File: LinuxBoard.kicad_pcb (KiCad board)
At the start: 2 copper layers, 182 parts, among them J1 Wuerth_7499010121A, J2 Conn_02x10_Counter_Clockwise, J3 Micro_SD_Card, J4 USB_A, J5 Conn_ARM_JTAG_SWD_20, J6 USB_B_Micro, SW1 SW_DIP_x03, SW2 SW_Push, SW3 SW_Push, SW4 SW_Push, SW5 SW_Push, U1 STM32MP151AAB3, U2 MT41K64M16TW-107_AAT_J_TR, U3 DP83848C, U4 STPMIC1APQR, Y1 24MHz, Y2 32.768KHz, Y2 Crystal_GND24, Y3 25MHz

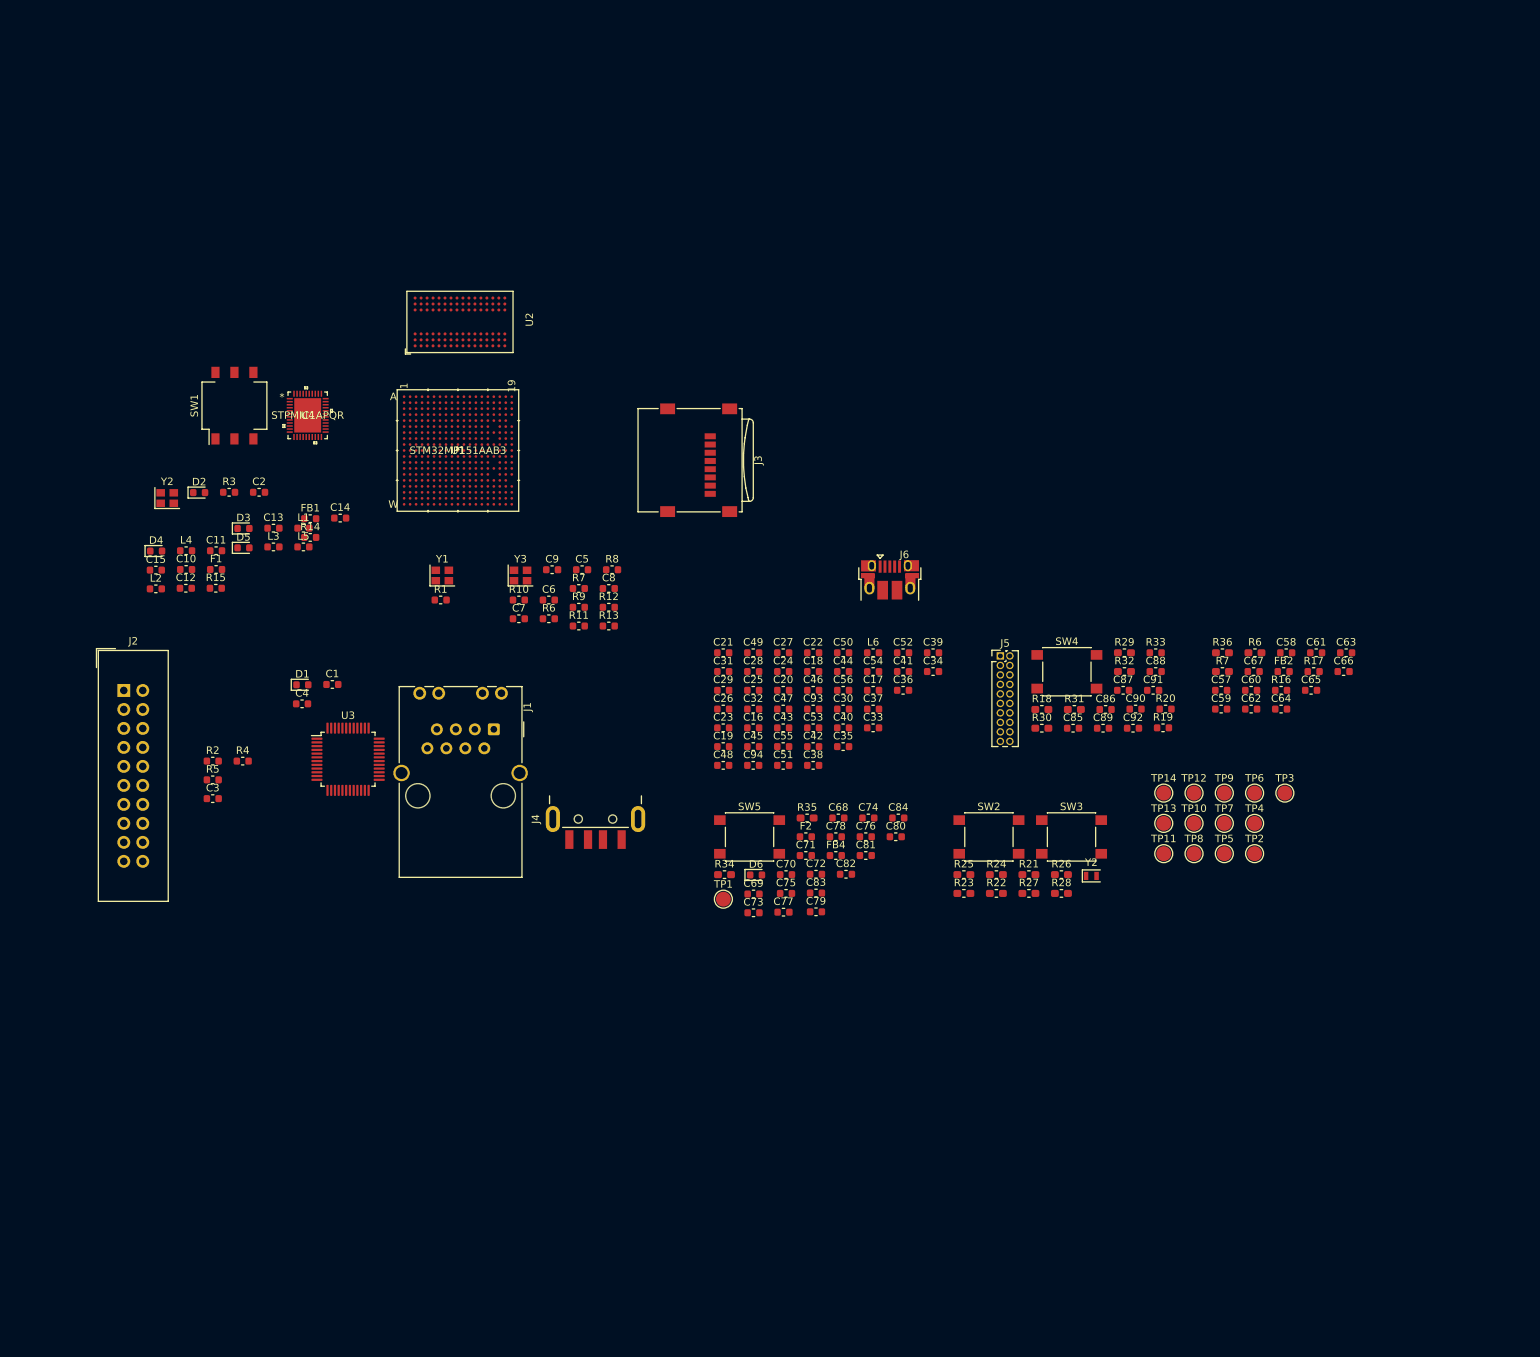
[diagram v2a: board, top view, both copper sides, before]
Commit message: Update jtag connector to swd
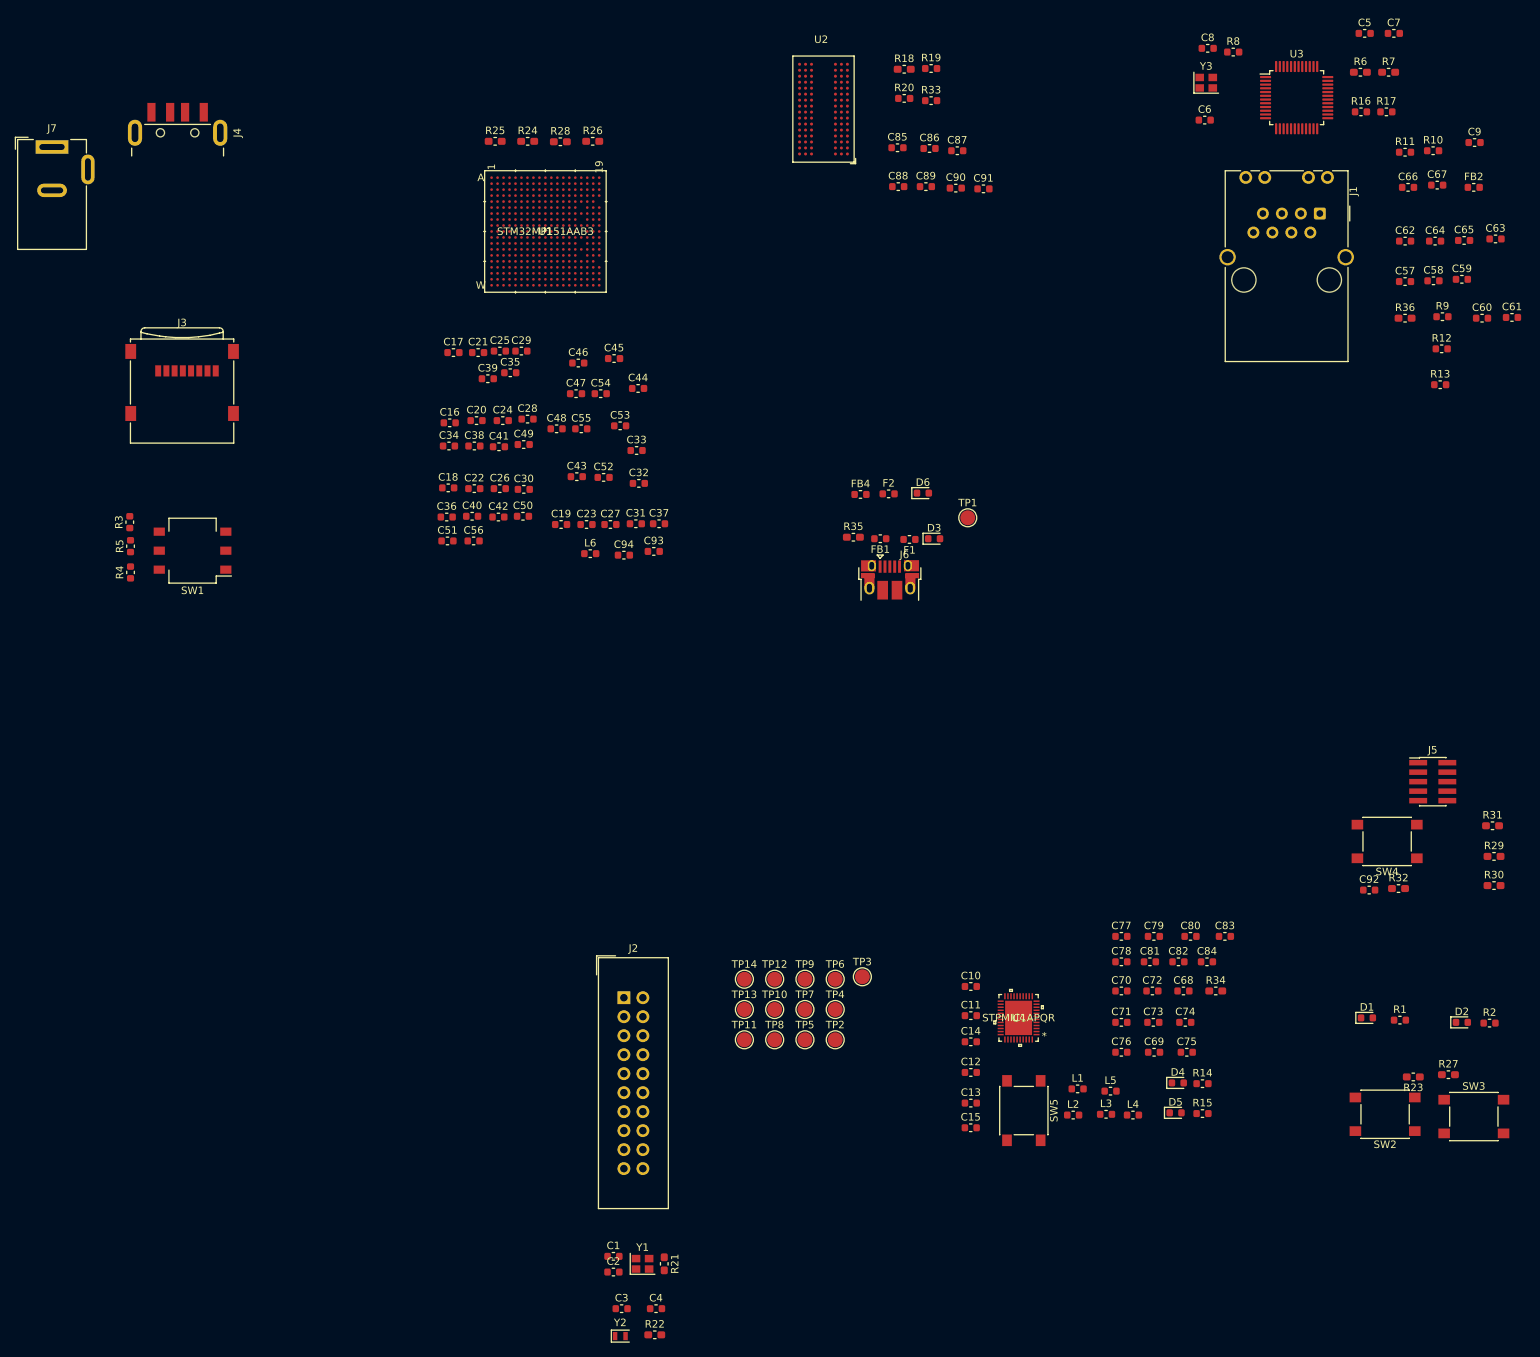
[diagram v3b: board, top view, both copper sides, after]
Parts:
- removed the R6 at (152.9, 92.1)
- removed the R7 at (156.9, 88.1)
- removed the Y2 at (101.8, 76.0)
- added J7: Barrel_Jack, Connector_BarrelJack:BarrelJack_Wuerth_6941xx301002, F.Cu at (86.4, 29.0)
- J5: value Conn_ARM_JTAG_SWD_20 -> Conn_ARM_JTAG_SWD_10; footprint Connector_PinHeader_1.27mm:PinHeader_2x10_P1.27mm_Vertical -> Connector_PinHeader_1.27mm:PinHeader_2x05_P1.27mm_Vertical_SMD
- moved D2 183.2 mm to (275.0, 146.1)
- moved R2 174.4 mm to (278.7, 146.2)
- moved U3 154.7 mm to (252.9, 22.4)
- moved D4 154.1 mm to (237.0, 154.2)
- moved R15 149.5 mm to (240.3, 158.3)
- moved D1 149.2 mm to (262.3, 145.5)
- moved L4 147.4 mm to (231.0, 158.5)
- moved D5 145.8 mm to (236.7, 158.2)
- moved L2 141.5 mm to (223.0, 158.5)
- moved C7 140.8 mm to (265.9, 13.8)
- moved R1 140.1 mm to (266.7, 145.8)
- moved R14 140.0 mm to (240.3, 154.3)
- moved R10 136.3 mm to (271.1, 29.5)
- moved C9 136.0 mm to (276.7, 28.4)
- moved L3 134.8 mm to (227.4, 158.4)
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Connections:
- J5 pad 10: GND -> /RAM/NRST
- J5 pad 2: /VDD -> /RAM/SWDIO
- J5 pad 3: /RAM/NJTRST -> GND
- J5 pad 4: GND -> /RAM/SWDCLK
- J5 pad 5: /RAM/JTDI -> GND
- J5 pad 6: GND -> /RAM/SWO
- J5 pad 7: /RAM/SWDIO -> Net-(J5-Pad7)
- J5 pad 8: GND -> Net-(J5-Pad8)
- J5 pad 9: /RAM/SWDCLK -> GND
- U1 pad D12: /RAM/NJTRST -> Net-(U1-PadD12)
- U1 pad D13: /RAM/JTDI -> Net-(U1-PadD13)
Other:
- copper layers 2 -> 4

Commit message: Fix footprints
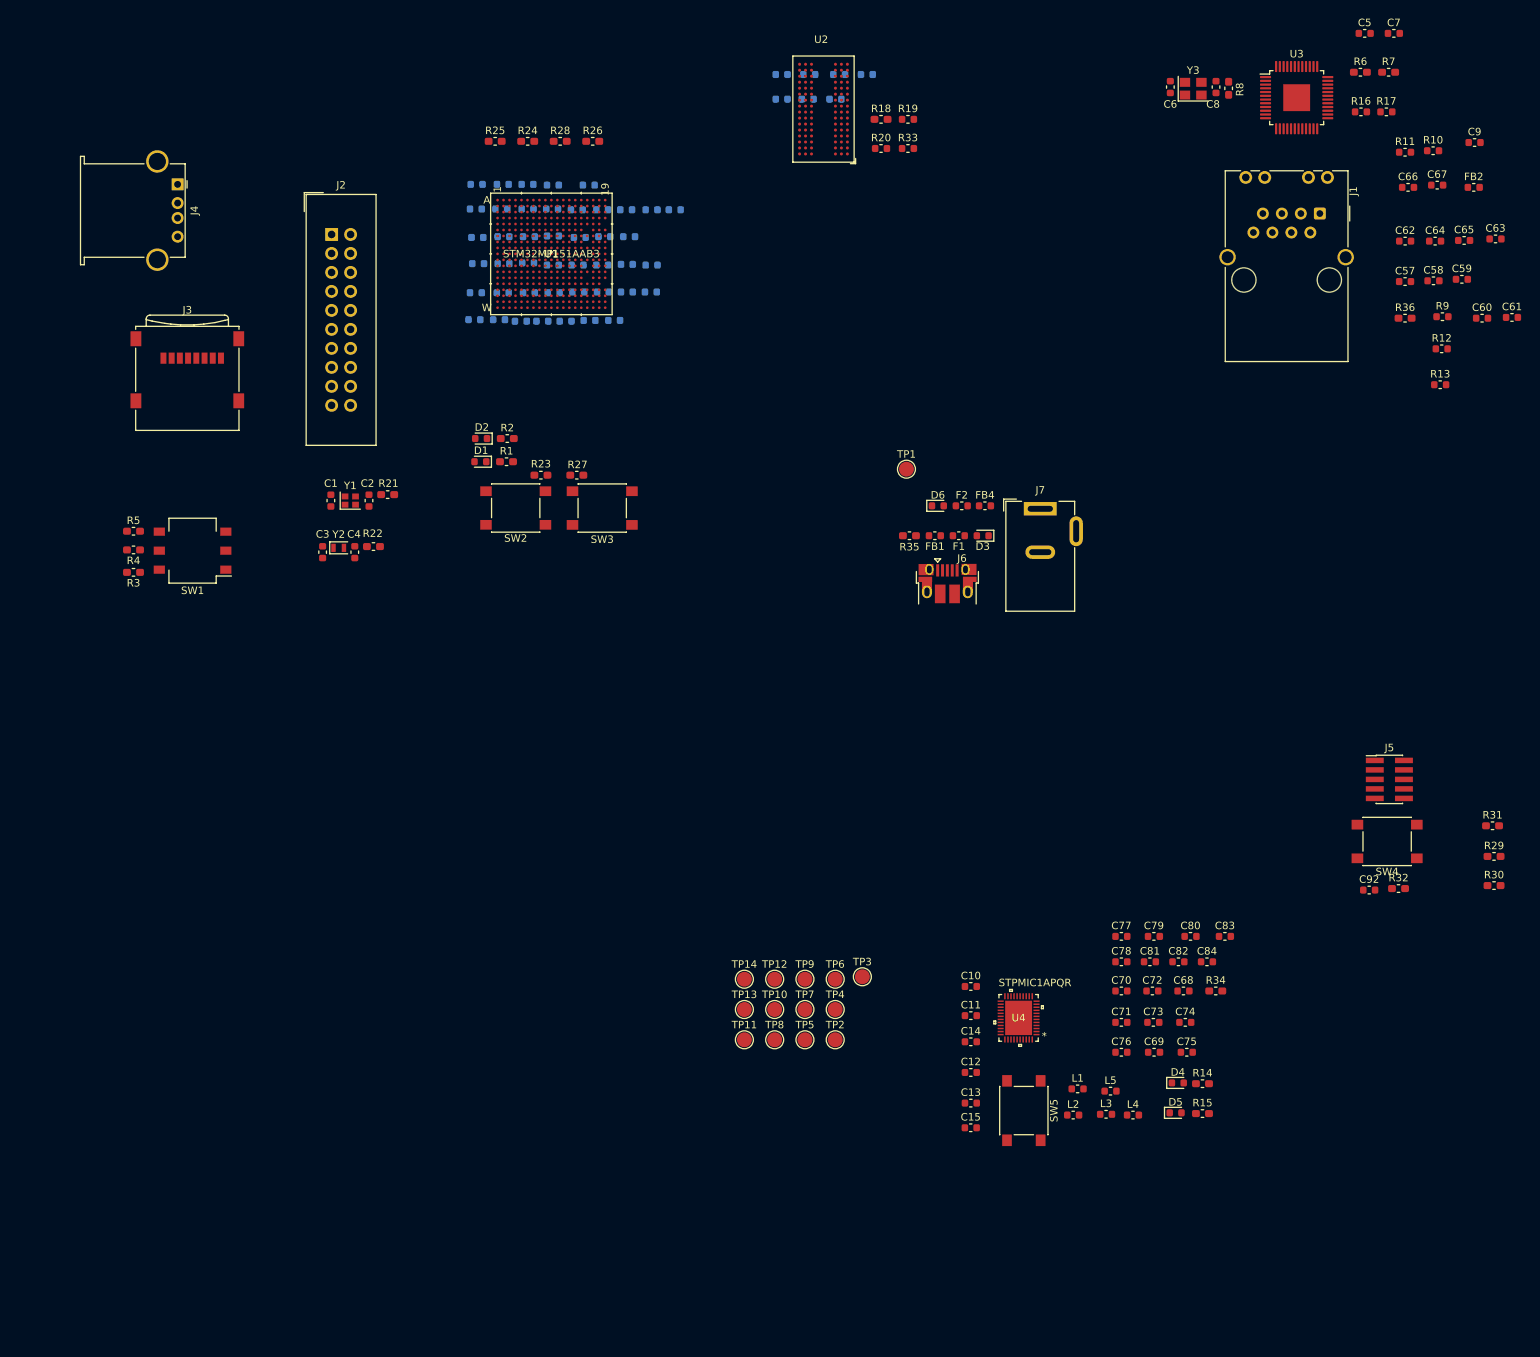
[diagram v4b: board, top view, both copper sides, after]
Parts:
- C16, C17, C18, C19, C20, C21, C22, C23, C24, C25, C26, C27, C28, C29, C30, C31, C32, C33, C34, C35, C36, C37, C38, C39, C40, C41, C42, C43, C44, C45, C46, C47, C48, C49, C50, C51, C52, C53, C54, C55, C56, C85, C86, C87, C88, C89, C90, C91, C93, C94, L6: moved to B.Cu
- J4: footprint Connector_USB:USB_A_CNCTech_1001-011-01101_Horizontal -> Connector_USB:USB_A_Stewart_SS-52100-001_Horizontal
- J7: value Barrel_Jack -> Barrel_Jack_Switch
- R1, R14, R15, R2, R3, R4, R5, R8: footprint Resistor_SMD:R_0603_1608Metric -> Resistor_SMD:R_0603_1608Metric_Pad1.05x0.95mm_HandSolder
- U3: footprint Package_QFP:LQFP-48_7x7mm_P0.5mm -> Package_QFP:LQFP-48-1EP_7x7mm_P0.5mm_EP3.6x3.6mm
- Y1: footprint Crystal:Crystal_SMD_2520-4Pin_2.5x2.0mm -> Crystal:Crystal_SMD_2016-4Pin_2.0x1.6mm
- Y3: footprint Crystal:Crystal_SMD_2520-4Pin_2.5x2.0mm -> Crystal:Crystal_SMD_3225-4Pin_3.2x2.5mm
- moved R2 152.9 mm to (147.3, 68.0)
- moved D2 152.7 mm to (143.8, 68.0), turned to 180 degrees
- moved SW3 142.2 mm to (160.0, 77.3)
- moved SW2 141.8 mm to (148.4, 77.3)
- moved R23 141.8 mm to (151.8, 72.9), turned to 0 degrees
- moved R27 141.5 mm to (156.6, 72.9), turned to 180 degrees
- moved R1 140.9 mm to (147.2, 71.1)
- moved J7 140.8 mm to (218.6, 77.4)
- moved D1 140.0 mm to (143.7, 71.1), turned to 180 degrees
- moved Y2 112.0 mm to (124.8, 82.6)
- moved R22 112.0 mm to (129.4, 82.5), turned to 180 degrees
- moved R21 109.3 mm to (131.3, 75.5), turned to 180 degrees
- moved J2 109.3 mm to (123.8, 40.7)
- moved Y1 109.3 mm to (126.3, 76.3)
- moved C4 108.9 mm to (126.9, 83.2), turned to 270 degrees
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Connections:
- J7 pad 3: (no net) -> GND

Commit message: Add mounting holes
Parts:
- R18, R19, R20, R33: moved to B.Cu
- moved J1 211.4 mm to (53.0, 96.8), turned to 180 degrees
- moved C61 199.3 mm to (87.2, 95.5), turned to 270 degrees
- moved U3 197.7 mm to (68.5, 93.7), turned to 270 degrees
- moved R13 195.5 mm to (78.2, 85.9), turned to 270 degrees
- moved C60 194.7 mm to (87.1, 91.5), turned to 270 degrees
- moved R12 191.7 mm to (83.0, 86.1), turned to 270 degrees
- moved C63 189.1 mm to (97.7, 93.3), turned to 270 degrees
- moved R9 188.3 mm to (87.3, 86.2), turned to 270 degrees
- moved C59 187.5 mm to (92.3, 88.8), turned to 270 degrees
- moved J7 185.7 mm to (48.2, 151.1), turned to 270 degrees
- moved R8 185.3 mm to (69.8, 84.6), turned to 0 degrees
- moved R17 184.4 mm to (87.8, 75.6), turned to 270 degrees
- moved C65 184.1 mm to (97.5, 89.1), turned to 270 degrees
- moved C58 183.1 mm to (92.1, 85.0), turned to 270 degrees
- moved C8 183.0 mm to (69.9, 82.9), turned to 180 degrees
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
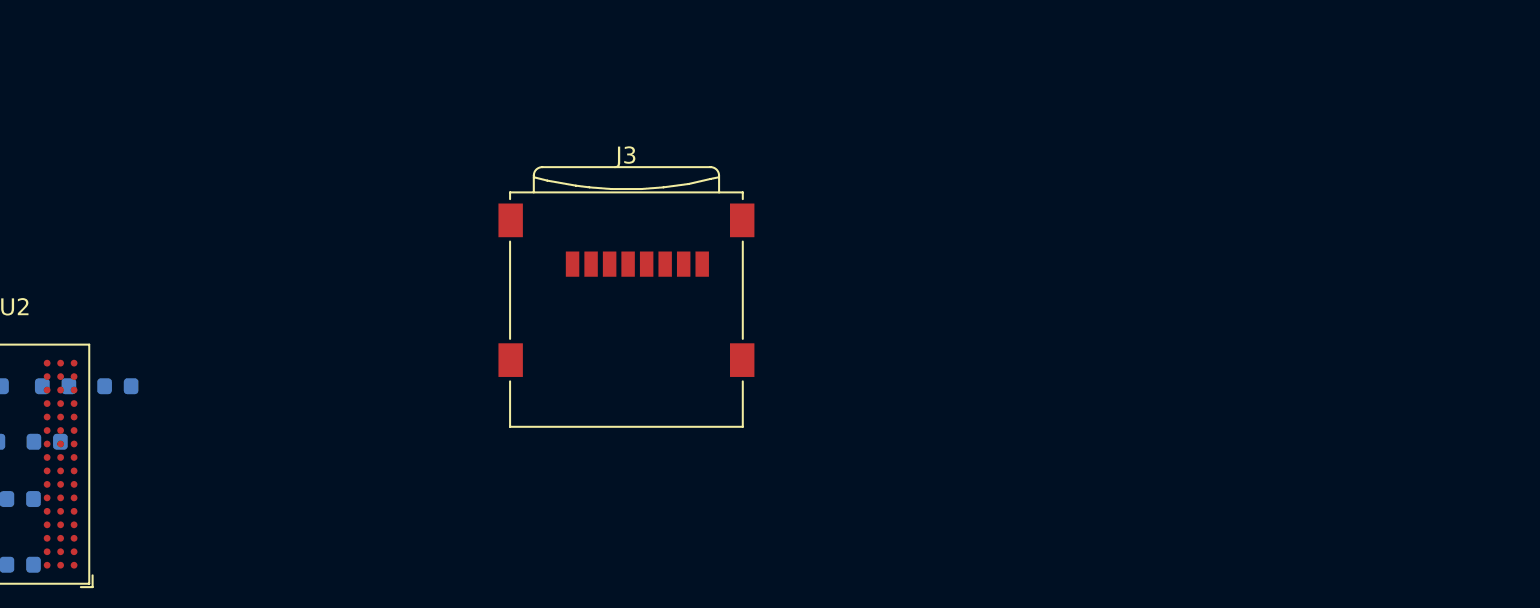
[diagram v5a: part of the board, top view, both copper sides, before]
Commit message: Add termination
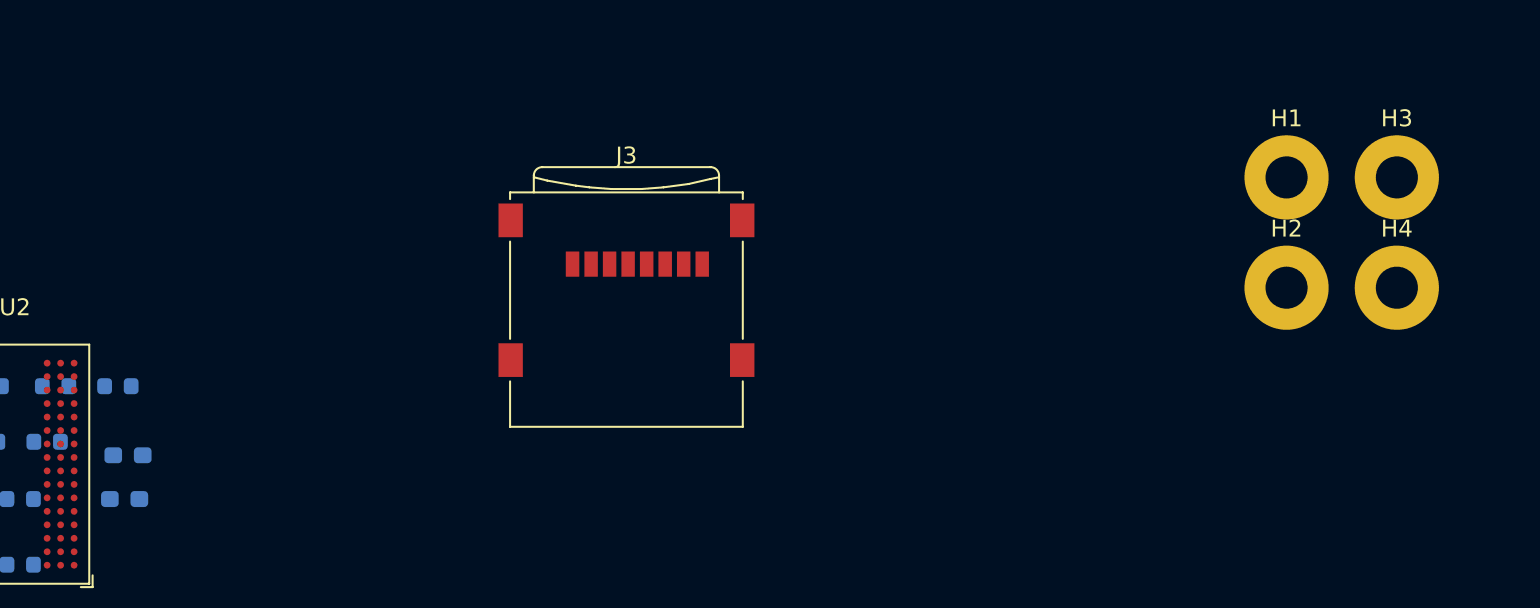
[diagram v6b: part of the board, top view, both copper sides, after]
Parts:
- added H1: MountingHole_Pad, MountingHole:MountingHole_2.5mm_Pad, F.Cu at (190.7, 108.5)
- added H2: MountingHole_Pad, MountingHole:MountingHole_2.5mm_Pad, F.Cu at (190.7, 115.0)
- added H3: MountingHole_Pad, MountingHole:MountingHole_2.5mm_Pad, F.Cu at (197.2, 108.5)
- added H4: MountingHole_Pad, MountingHole:MountingHole_2.5mm_Pad, F.Cu at (197.2, 115.0)
- added R29: 10k, Resistor_SMD:R_0603_1608Metric_Pad1.05x0.95mm_HandSolder, B.Cu at (121.7, 127.6)
- added R30: 100, Resistor_SMD:R_0603_1608Metric_Pad1.05x0.95mm_HandSolder, B.Cu at (121.9, 125.0)
- F1, F2: value Fuse -> 3A
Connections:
- U1 pad T12: Net-(U1-PadT12) -> /MPU/I2C_SCL
